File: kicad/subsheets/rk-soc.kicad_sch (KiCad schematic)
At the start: 24 parts, among them U5 RK3566

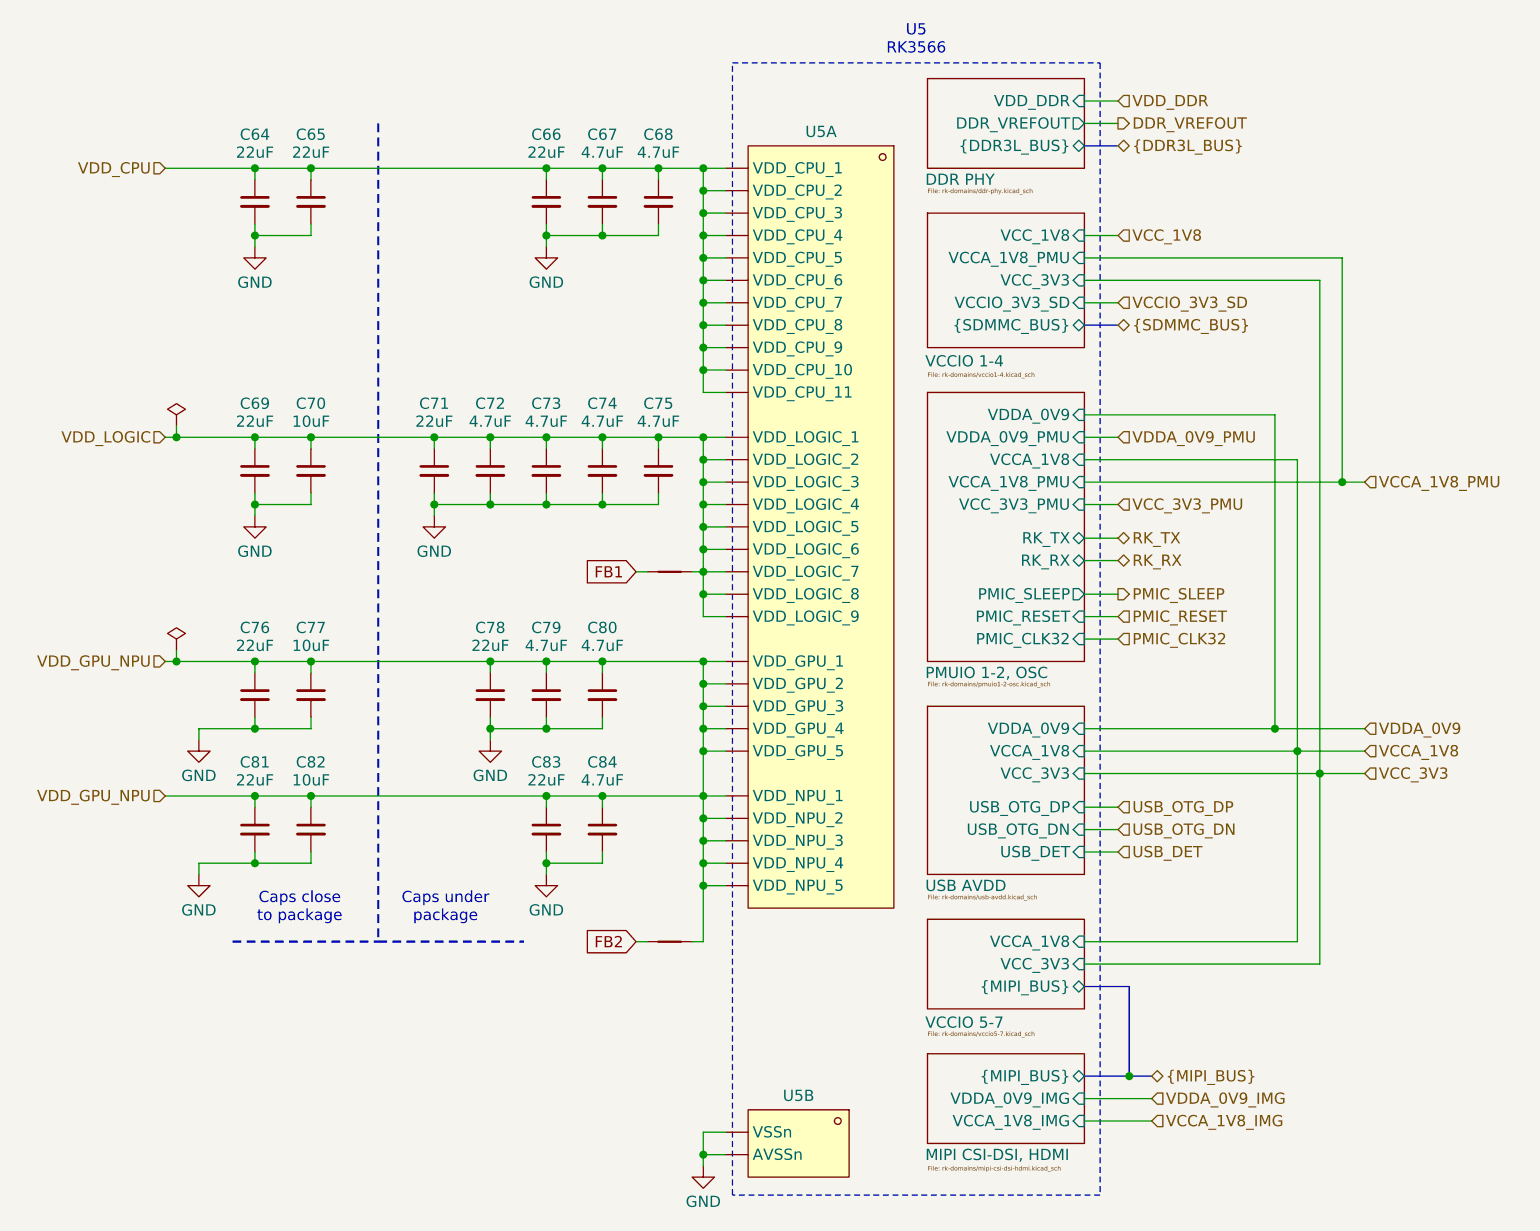
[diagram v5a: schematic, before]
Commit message: Remove power/decoupling for unused power domains
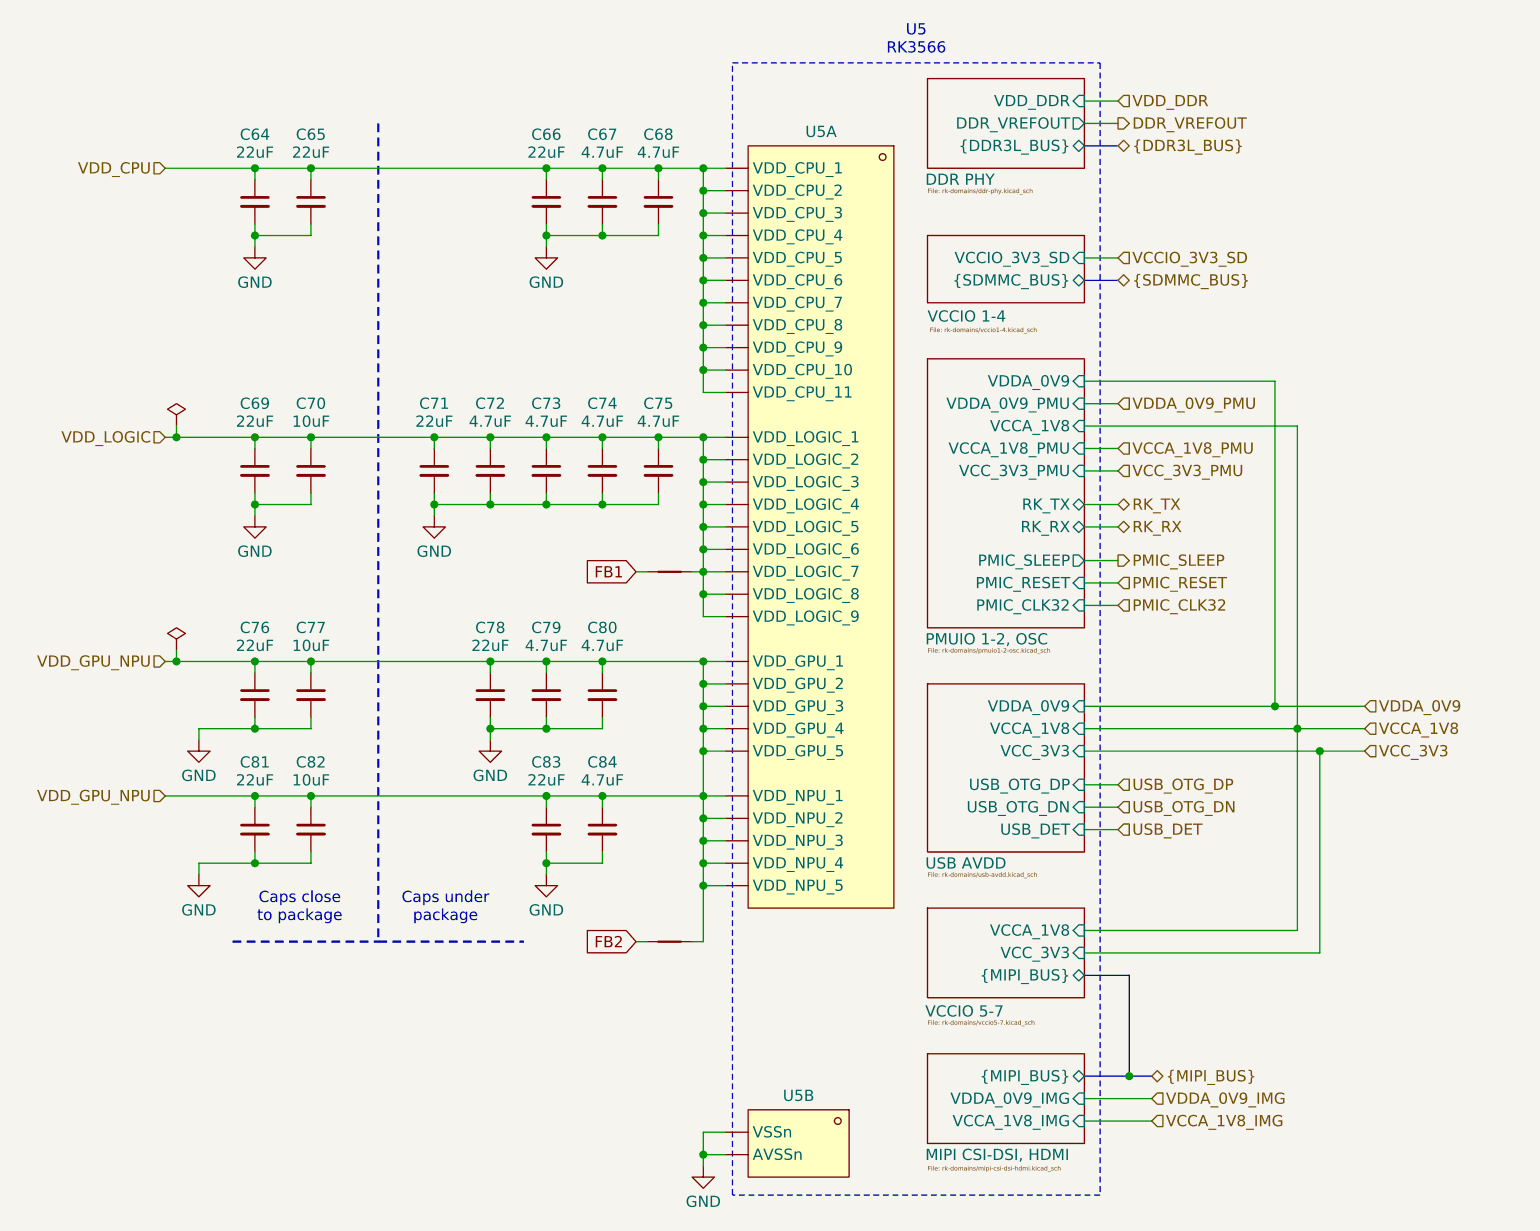
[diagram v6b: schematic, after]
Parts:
- renumbered NT5 to NT3, NT6 to NT4
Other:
- sheet VCCIO 1-4 ports: added none; removed VCCA_1V8_PMU, VCC_1V8, VCC_3V3

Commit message: All major components placed on board
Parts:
- C67, C68, C72, C73, C74, C75, C79, C80, C84: footprint Capacitor_SMD:C_0805_2012Metric -> Capacitor_SMD:C_0402_1005Metric
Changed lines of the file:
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@@
 			)
 		)
-		(property "Footprint" "Capacitor_SMD:C_0805_2012Metric"
+		(property "Footprint" "Capacitor_SMD:C_0402_1005Metric"
 			(at 119.38 76.2 0)
 			(effects
@@
 			)
 		)
-		(property "Footprint" "Capacitor_SMD:C_0805_2012Metric"
+		(property "Footprint" "Capacitor_SMD:C_0402_1005Metric"
 			(at 106.68 76.2 0)
 			(effects
@@
 			)
 		)
-		(property "Footprint" "Capacitor_SMD:C_0805_2012Metric"
+		(property "Footprint" "Capacitor_SMD:C_0402_1005Metric"
 			(at 113.03 116.84 0)
 			(effects
@@
 			)
 		)
-		(property "Footprint" "Capacitor_SMD:C_0805_2012Metric"
+		(property "Footprint" "Capacitor_SMD:C_0402_1005Metric"
 			(at 119.38 45.72 0)
 			(effects
@@
 			)
 		)
-		(property "Footprint" "Capacitor_SMD:C_0805_2012Metric"
+		(property "Footprint" "Capacitor_SMD:C_0402_1005Metric"
 			(at 113.03 101.6 0)
 			(effects
@@
 			)
 		)
-		(property "Footprint" "Capacitor_SMD:C_0805_2012Metric"
+		(property "Footprint" "Capacitor_SMD:C_0402_1005Metric"
 			(at 113.03 76.2 0)
 			(effects
@@
 			)
 		)
-		(property "Footprint" "Capacitor_SMD:C_0805_2012Metric"
+		(property "Footprint" "Capacitor_SMD:C_0402_1005Metric"
 			(at 100.33 76.2 0)
 			(effects
@@
 			)
 		)
-		(property "Footprint" "Capacitor_SMD:C_0805_2012Metric"
+		(property "Footprint" "Capacitor_SMD:C_0402_1005Metric"
 			(at 113.03 45.72 0)
 			(effects
@@
 			)
 		)
-		(property "Footprint" "Capacitor_SMD:C_0805_2012Metric"
+		(property "Footprint" "Capacitor_SMD:C_0402_1005Metric"
 			(at 106.68 101.6 0)
 			(effects
